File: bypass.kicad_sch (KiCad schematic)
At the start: 7 parts

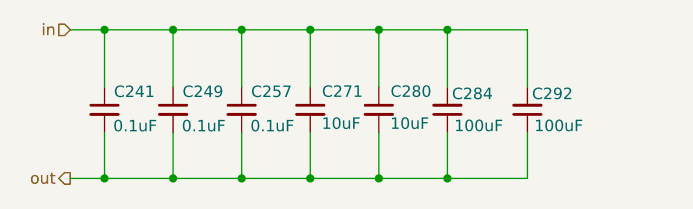
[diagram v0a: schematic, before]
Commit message: made the board double wide. rough ASIC and vreg placement.
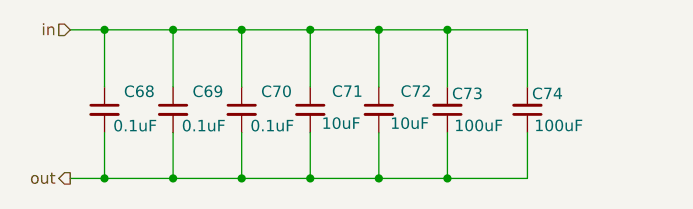
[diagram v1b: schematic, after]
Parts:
- renumbered C241 to C68, C249 to C69, C257 to C70, C271 to C71, C280 to C72, C284 to C73, C292 to C74

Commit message: ASICs placed. most other parts placed.
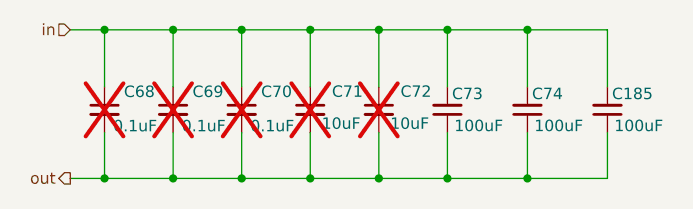
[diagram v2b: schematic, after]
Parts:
- added C185: 100uF, Capacitor_SMD:C_1206_3216Metric, symbol Device:C_Small
- C68, C69, C70, C71, C72: now not fitted; now left out of the parts list
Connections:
- net in: now also C185.2
- net out: now also C185.1
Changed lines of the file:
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@@
+	)
+	(junction
+		(at 166.37 90.17)
+		(diameter 0)
+		(color 0 0 0 0)
 	)
 	(junction
@@
 	)
 	(junction
+		(at 166.37 73.66)
+		(diameter 0)
+		(color 0 0 0 0)
+	)
+	(junction
 		(at 142.24 73.66)
 		(diameter 0)
@@
 	(wire
 		(pts
+			(xy 175.26 90.17) (xy 166.37 90.17)
+		)
+		(stroke
+			(width 0)
+			(type default)
+		)
+	)
+	(wire
+		(pts
 			(xy 149.86 73.66) (xy 142.24 73.66)
 		)
@@
 	(wire
 		(pts
+			(xy 175.26 85.09) (xy 175.26 90.17)
+		)
+		(stroke
+			(width 0)
+			(type default)
+		)
+	)
+	(wire
+		(pts
 			(xy 157.48 73.66) (xy 149.86 73.66)
 		)
@@
 		(pts
 			(xy 127 85.09) (xy 127 90.17)
+		)
+		(stroke
+			(width 0)
+			(type default)
+		)
+	)
+	(wire
+		(pts
+			(xy 175.26 80.01) (xy 175.26 73.66)
+		)
+		(stroke
+			(width 0)
+			(type default)
+		)
+	)
+	(wire
+		(pts
+			(xy 166.37 73.66) (xy 175.26 73.66)
 		)
 		(stroke
@@
 	(symbol
 		(lib_id "Device:C_Small")
-		(at 119.38 82.55 0)
-		(mirror y)
+		(at 175.26 82.55 180)
 		(unit 1)
 		(exclude_from_sim no)
@@
 		(on_board yes)
 		(dnp no)
+		(property "Reference" "C185"
+			(at 175.768 80.772 0)
+			(effects
+				(font
+					(size 1.27 1.27)
+				)
+				(justify right)
+			)
+		)
+		(property "Value" "100uF"
+			(at 176.022 84.328 0)
+			(effects
+				(font
+					(size 1.27 1.27)
+				)
+				(justify right)
+			)
+		)
+		(property "Footprint" "Capacitor_SMD:C_1206_3216Metric"
+			(at 175.26 82.55 0)
+			(effects
+				(font
+					(size 1.27 1.27)
+				)
+				(hide yes)
+			)
+		)
+		(property "Datasheet" "~"
+			(at 175.26 82.55 0)
+			(effects
+				(font
+					(size 1.27 1.27)
+				)
+				(hide yes)
+			)
+		)
+		(property "Description" "Unpolarized capacitor, small symbol"
+			(at 175.26 82.55 0)
+			(effects
+				(font
+					(size 1.27 1.27)
+				)
+				(hide yes)
+			)
+		)
+		(property "voltage" "6.3V"
+			(at 179.578 85.852 0)
+			(effects
+				(font
+					(size 1.27 1.27)
+				)
+				(hide yes)
+			)
+		)
+		(property "PARTNO" "CL31A107MQHNNNE"
+			(at 175.26 82.55 0)
+			(effects
+				(font
+					(size 1.27 1.27)
+				)
+				(hide yes)
+			)
+		)
+		(property "DK" "1276-1782-1-ND"
+			(at 175.26 82.55 0)
+			(effects
+				(font
+					(size 1.27 1.27)
+				)
+				(hide yes)
+			)
+		)
+		(property "partnum" ""
+			(at 175.26 82.55 0)
+			(effects
+				(font
+					(size 1.27 1.27)
+				)
+				(hide yes)
+			)
+		)
+		(property "Power" ""
+			(at 175.26 82.55 0)
+			(effects
+				(font
+					(size 1.27 1.27)
+				)
+			)
+		)
+		(pin "1"
+		)
+		(pin "2"
+		)
+		(instances
+			(project "BitaxeBonanza"
+				(path "/61fe8d2c-9301-4ad9-8caf-c47acfa835b0/5053a6d5-ae8d-4ae0-9f6e-0d65e80da719/1839dd6a-6da4-43e4-869e-5f1c3a692dae"
+					(reference "C185")
+					(unit 1)
+				)
+				(path "/61fe8d2c-9301-4ad9-8caf-c47acfa835b0/5053a6d5-ae8d-4ae0-9f6e-0d65e80da719/25011f59-b197-4b80-9e13-50bcd8397584"
+					(reference "C188")
+					(unit 1)
+				)
+				(path "/61fe8d2c-9301-4ad9-8caf-c47acfa835b0/5053a6d5-ae8d-4ae0-9f6e-0d65e80da719/266ca2b6-aa4d-437e-a783-4ce8fb6679e3"
+					(reference "C195")
+					(unit 1)
+				)
+				(path "/61fe8d2c-9301-4ad9-8caf-c47acfa835b0/5053a6d5-ae8d-4ae0-9f6e-0d65e80da719/4568b792-dd60-4ded-b65e-eeab7d0b21e1"
+					(reference "C196")
+					(unit 1)
+				)
+				(path "/61fe8d2c-9301-4ad9-8caf-c47acfa835b0/5053a6d5-ae8d-4ae0-9f6e-0d65e80da719/52ff0721-58be-44aa-874b-18af8ecc5e1a"
+					(reference "C198")
+					(unit 1)
+				)
+				(path "/61fe8d2c-9301-4ad9-8caf-c47acfa835b0/5053a6d5-ae8d-4ae0-9f6e-0d65e80da719/59ff3b46-ff6d-4c90-9b1d-f478b842ed95"
+					(reference "C189")
+					(unit 1)
+				)
+				(path "/61fe8d2c-9301-4ad9-8caf-c47acfa835b0/5053a6d5-ae8d-4ae0-9f6e-0d65e80da719/6bd2f899-c307-419e-ace6-93ee2d17c7cc"
+					(reference "C192")
+					(unit 1)
+				)
+				(path "/61fe8d2c-9301-4ad9-8caf-c47acfa835b0/5053a6d5-ae8d-4ae0-9f6e-0d65e80da719/7182e5f5-7c1f-4907-b066-063f65254832"
+					(reference "C187")
+					(unit 1)
+				)
+				(path "/61fe8d2c-9301-4ad9-8caf-c47acfa835b0/5053a6d5-ae8d-4ae0-9f6e-0d65e80da719/840839b3-9095-406e-90e2-cc6e9ff653e1"
+					(reference "C200")
+					(unit 1)
+				)
+				(path "/61fe8d2c-9301-4ad9-8caf-c47acfa835b0/5053a6d5-ae8d-4ae0-9f6e-0d65e80da719/93ac77d4-9b75-4dc7-aa65-e503eb8b5007"
+					(reference "C193")
+					(unit 1)
+				)
+				(path "/61fe8d2c-9301-4ad9-8caf-c47acfa835b0/5053a6d5-ae8d-4ae0-9f6e-0d65e80da719/989dcc2d-abd6-4ecc-8579-1f93e51e9383"
+					(reference "C194")
+					(unit 1)
+				)
+				(path "/61fe8d2c-9301-4ad9-8caf-c47acfa835b0/5053a6d5-ae8d-4ae0-9f6e-0d65e80da719/a9c9f77a-8501-48b8-9a71-f3d2565cdb95"
+					(reference "C199")
+					(unit 1)
+				)
+				(path "/61fe8d2c-9301-4ad9-8caf-c47acfa835b0/5053a6d5-ae8d-4ae0-9f6e-0d65e80da719/b995a4b7-acde-4998-ab6f-b5236f488b5b"
+					(reference "C197")
+					(unit 1)
+				)
+				(path "/61fe8d2c-9301-4ad9-8caf-c47acfa835b0/5053a6d5-ae8d-4ae0-9f6e-0d65e80da719/e2beb58a-24ce-4062-a188-a172c045a96f"
+					(reference "C191")
+					(unit 1)
+				)
+				(path "/61fe8d2c-9301-4ad9-8caf-c47acfa835b0/5053a6d5-ae8d-4ae0-9f6e-0d65e80da719/e551e515-aca6-49a7-80d3-47c6c23e7831"
+					(reference "C190")
+					(unit 1)
+				)
+				(path "/61fe8d2c-9301-4ad9-8caf-c47acfa835b0/5053a6d5-ae8d-4ae0-9f6e-0d65e80da719/e7a3b23b-3e91-40f8-8eb1-74e6b1002e0e"
+					(reference "C186")
+					(unit 1)
+				)
+			)
+		)
+	)
+	(symbol
+		(lib_id "Device:C_Small")
+		(at 119.38 82.55 0)
+		(mirror y)
+		(unit 1)
+		(exclude_from_sim no)
+		(in_bom no)
+		(on_board no)
+		(dnp yes)
 		(property "Reference" "C68"
 			(at 124.968 81.28 0)
@@
 		(unit 1)
 		(exclude_from_sim no)
-		(in_bom yes)
-		(on_board yes)
-		(dnp no)
+		(in_bom no)
+		(on_board no)
+		(dnp yes)
 		(property "Reference" "C71"
 			(at 148.082 80.518 0)
@@
 		(unit 1)
 		(exclude_from_sim no)
-		(in_bom yes)
-		(on_board yes)
-		(dnp no)
+		(in_bom no)
+		(on_board no)
+		(dnp yes)
 		(property "Reference" "C70"
 			(at 140.208 81.28 0)
@@
 		(unit 1)
 		(exclude_from_sim no)
-		(in_bom yes)
-		(on_board yes)
-		(dnp no)
+		(in_bom no)
+		(on_board no)
+		(dnp yes)
 		(property "Reference" "C72"
 			(at 155.702 80.518 0)
@@
 		(unit 1)
 		(exclude_from_sim no)
-		(in_bom yes)
-		(on_board yes)
-		(dnp no)
+		(in_bom no)
+		(on_board no)
+		(dnp yes)
 		(property "Reference" "C69"
 			(at 132.588 81.28 0)

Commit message: switch to the bitaxeBIRDS based pre-bonanza
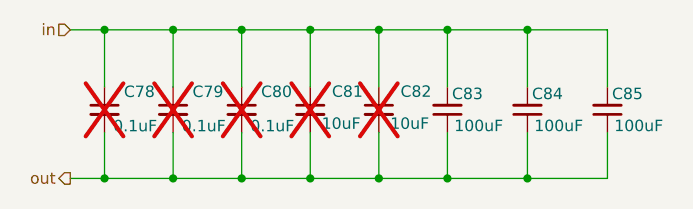
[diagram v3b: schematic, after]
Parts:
- C83: renamed from C73; footprint Capacitor_SMD:C_1206_3216Metric -> Capacitor_SMD:C_0805_2012Metric; DK 1276-1782-1-ND -> 490-GRM21BR60G107ME11KCT-ND; PARTNO CL31A107MQHNNNE -> GRM21BR60G107ME11K; voltage 6.3V -> 4V
- C84: renamed from C74; footprint Capacitor_SMD:C_1206_3216Metric -> Capacitor_SMD:C_0805_2012Metric; DK 1276-1782-1-ND -> 490-GRM21BR60G107ME11KCT-ND; PARTNO CL31A107MQHNNNE -> GRM21BR60G107ME11K; voltage 6.3V -> 4V
- C85: renamed from C185; footprint Capacitor_SMD:C_1206_3216Metric -> Capacitor_SMD:C_0805_2012Metric; DK 1276-1782-1-ND -> 490-GRM21BR60G107ME11KCT-ND; PARTNO CL31A107MQHNNNE -> GRM21BR60G107ME11K; voltage 6.3V -> 4V
- renumbered C68 to C78, C69 to C79, C70 to C80, C71 to C81, C72 to C82
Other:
- title: (none) -> bitaxeBonanza

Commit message: updated schematic worksheet
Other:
- company: (none) -> bitaxeorg
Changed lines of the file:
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@@
 		(date "2026-02-11")
 		(rev "1002x")
+		(company "bitaxeorg")
+		(comment 1 "OHL v2")
 	)
 	(junction
